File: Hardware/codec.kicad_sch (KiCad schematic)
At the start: 6 parts

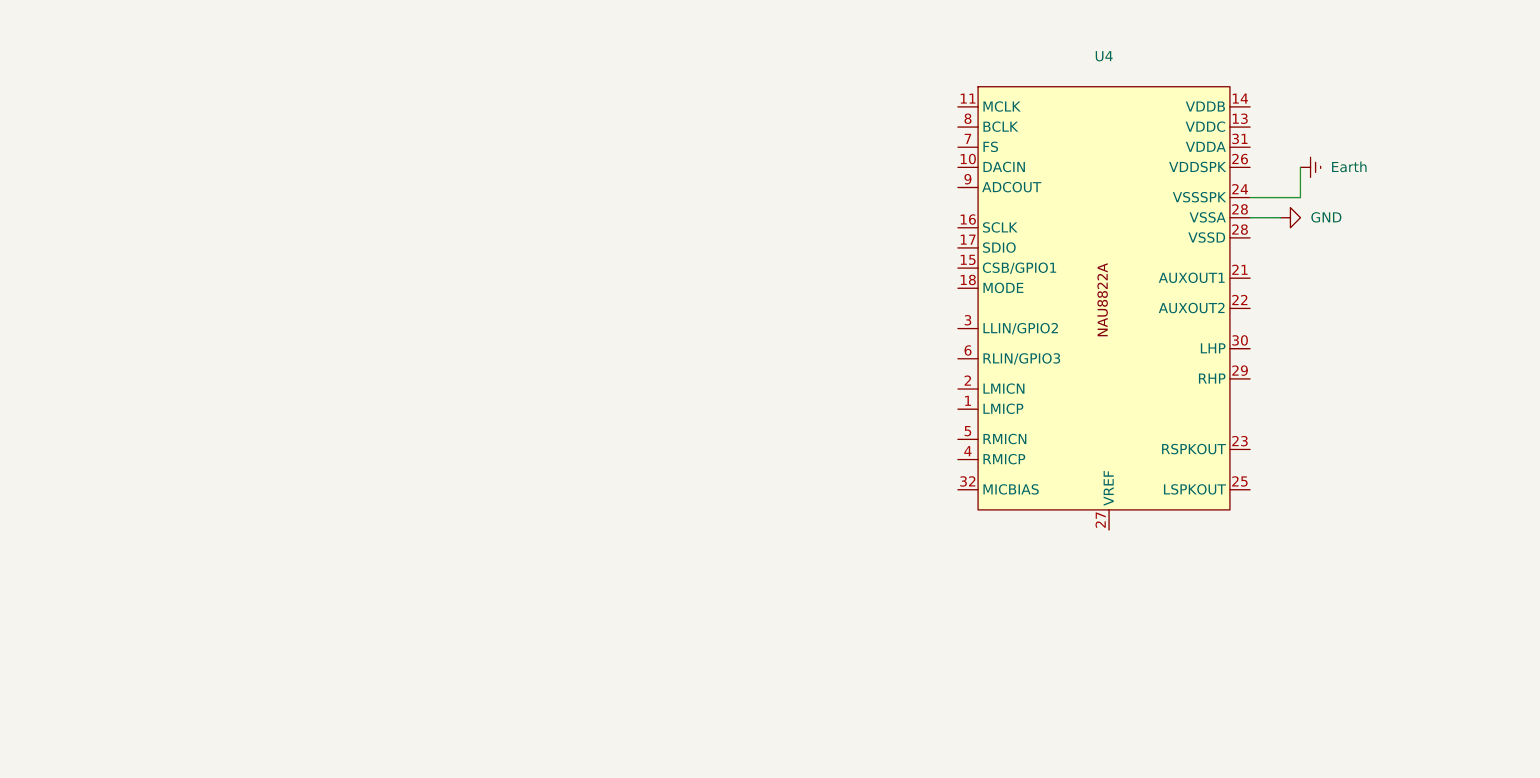
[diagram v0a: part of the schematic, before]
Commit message: CODEC schematics
Missing mic ins and all audio outputs.
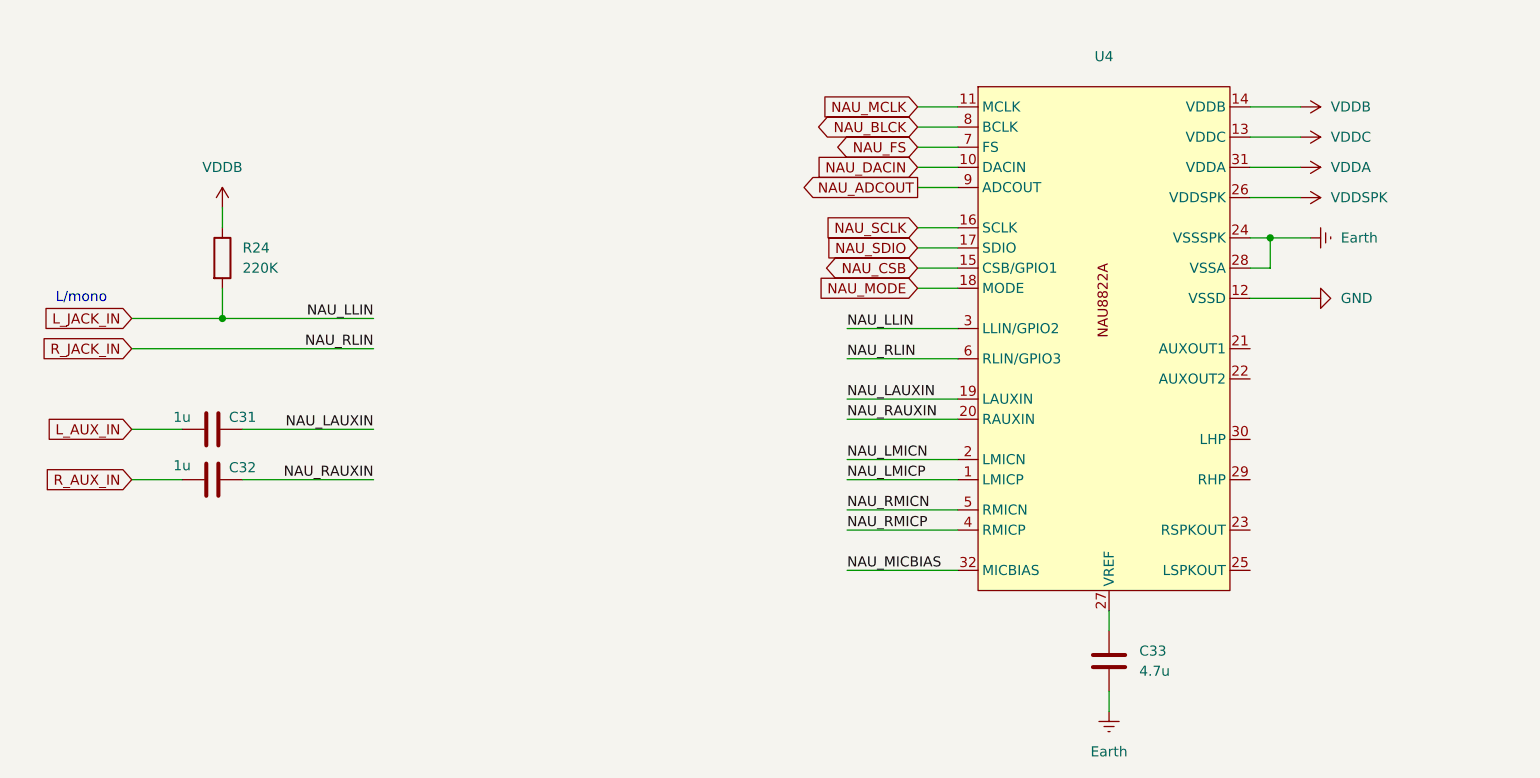
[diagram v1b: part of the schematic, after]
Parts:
- added C31, C32: 1u, symbol Device:C
- added C33: 4.7u, symbol Device:C
- added R24: 220K, symbol Device:R
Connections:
- net Earth: now also U4.28 (VSSA), C33.2
- net GND: now also U4.12 (VSSD); no longer U4.28 (VSSD)
- net VDDA: now also U4.31 (VDDA)
- net VDDB: now also U4.14 (VDDB), R24.1
- net VDDC: now also U4.13 (VDDC)
- net VDDSPK: now also U4.26 (VDDSPK)
- net NAU_LMICP: now reaches U4.1 (LMICP)
- net NAU_DACIN: now reaches U4.10 (DACIN)
- net NAU_MCLK: now reaches U4.11 (MCLK)
- net NAU_CSB: now reaches U4.15 (CSB/GPIO1)
- net NAU_SCLK: now reaches U4.16 (SCLK)
- net NAU_SDIO: now reaches U4.17 (SDIO)
- net NAU_MODE: now reaches U4.18 (MODE)
- net NAU_LMICN: now reaches U4.2 (LMICN)
- net at U4.27 (VREF): now also C33.1
- net L_JACK_IN: now reaches U4.3 (LLIN/GPIO2)
- net L_JACK_IN: now also R24.2
- net NAU_MICBIAS: now reaches U4.32 (MICBIAS)
- net NAU_RMICP: now reaches U4.4 (RMICP)
- net NAU_RMICN: now reaches U4.5 (RMICN)
- net R_JACK_IN: now reaches U4.6 (RLIN/GPIO3)
- net NAU_FS: now reaches U4.7 (FS)
- net NAU_BLCK: now reaches U4.8 (BCLK)
- net NAU_ADCOUT: now reaches U4.9 (ADCOUT)
- new net L_AUX_IN: C31.1
- new net NAU_LAUXIN: C31.2, U4.19 (LAUXIN)
- new net NAU_RAUXIN: C32.2, U4.20 (RAUXIN)
- new net R_AUX_IN: C32.1
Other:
- note added: "L/mono"

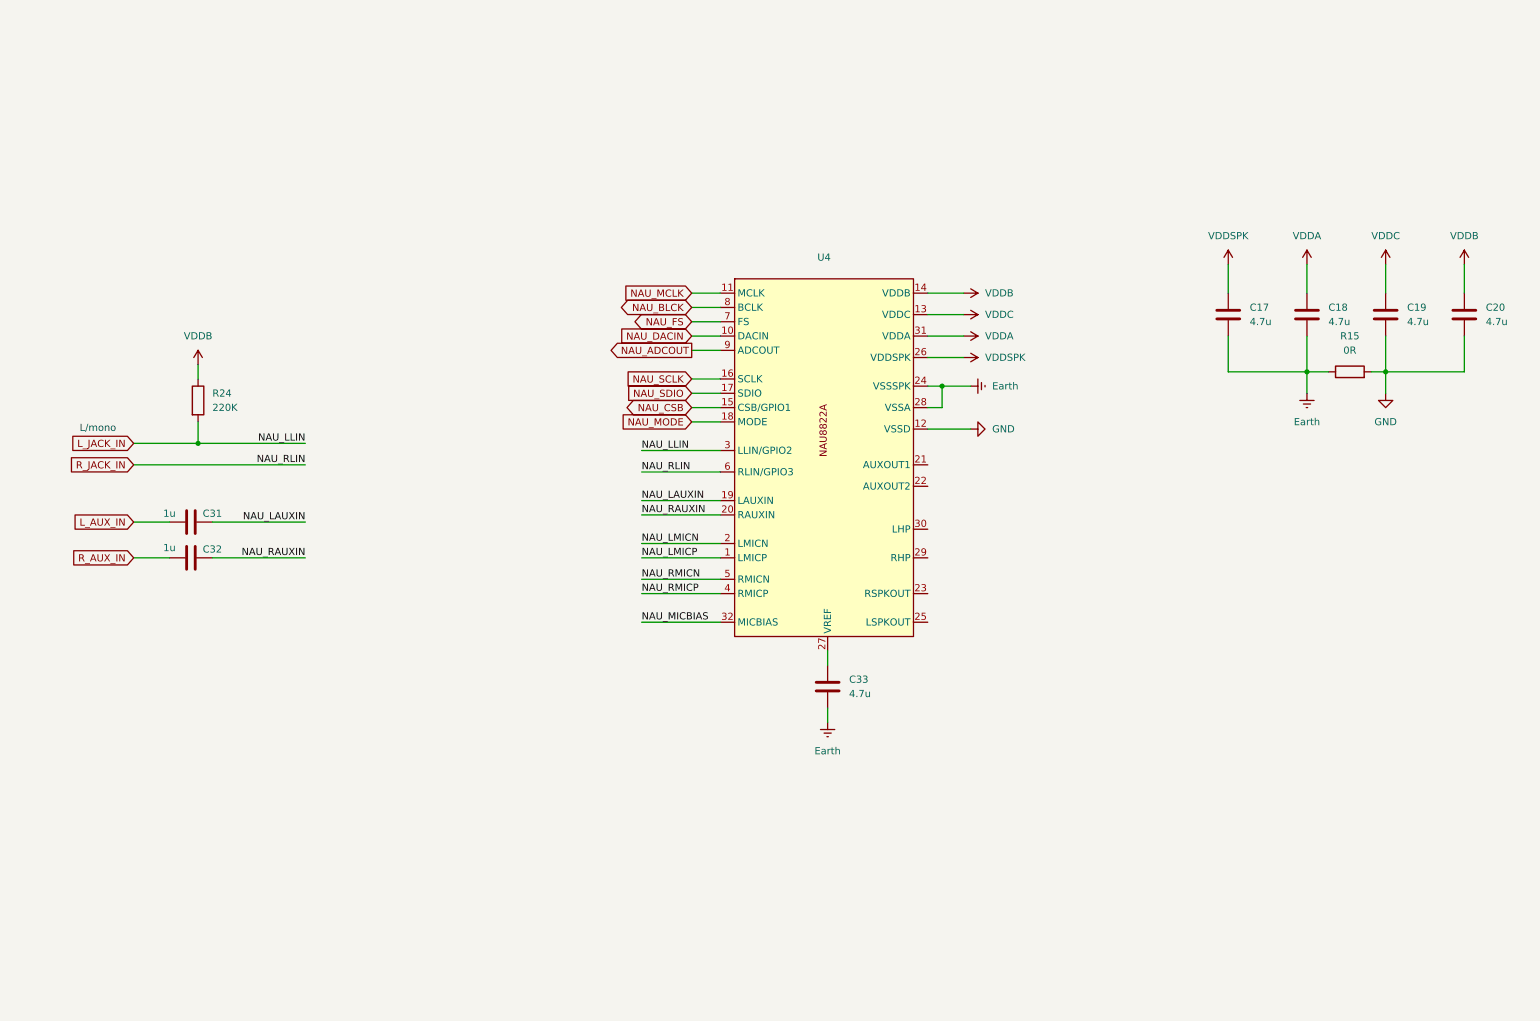
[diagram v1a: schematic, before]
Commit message: Codec schem ready for review
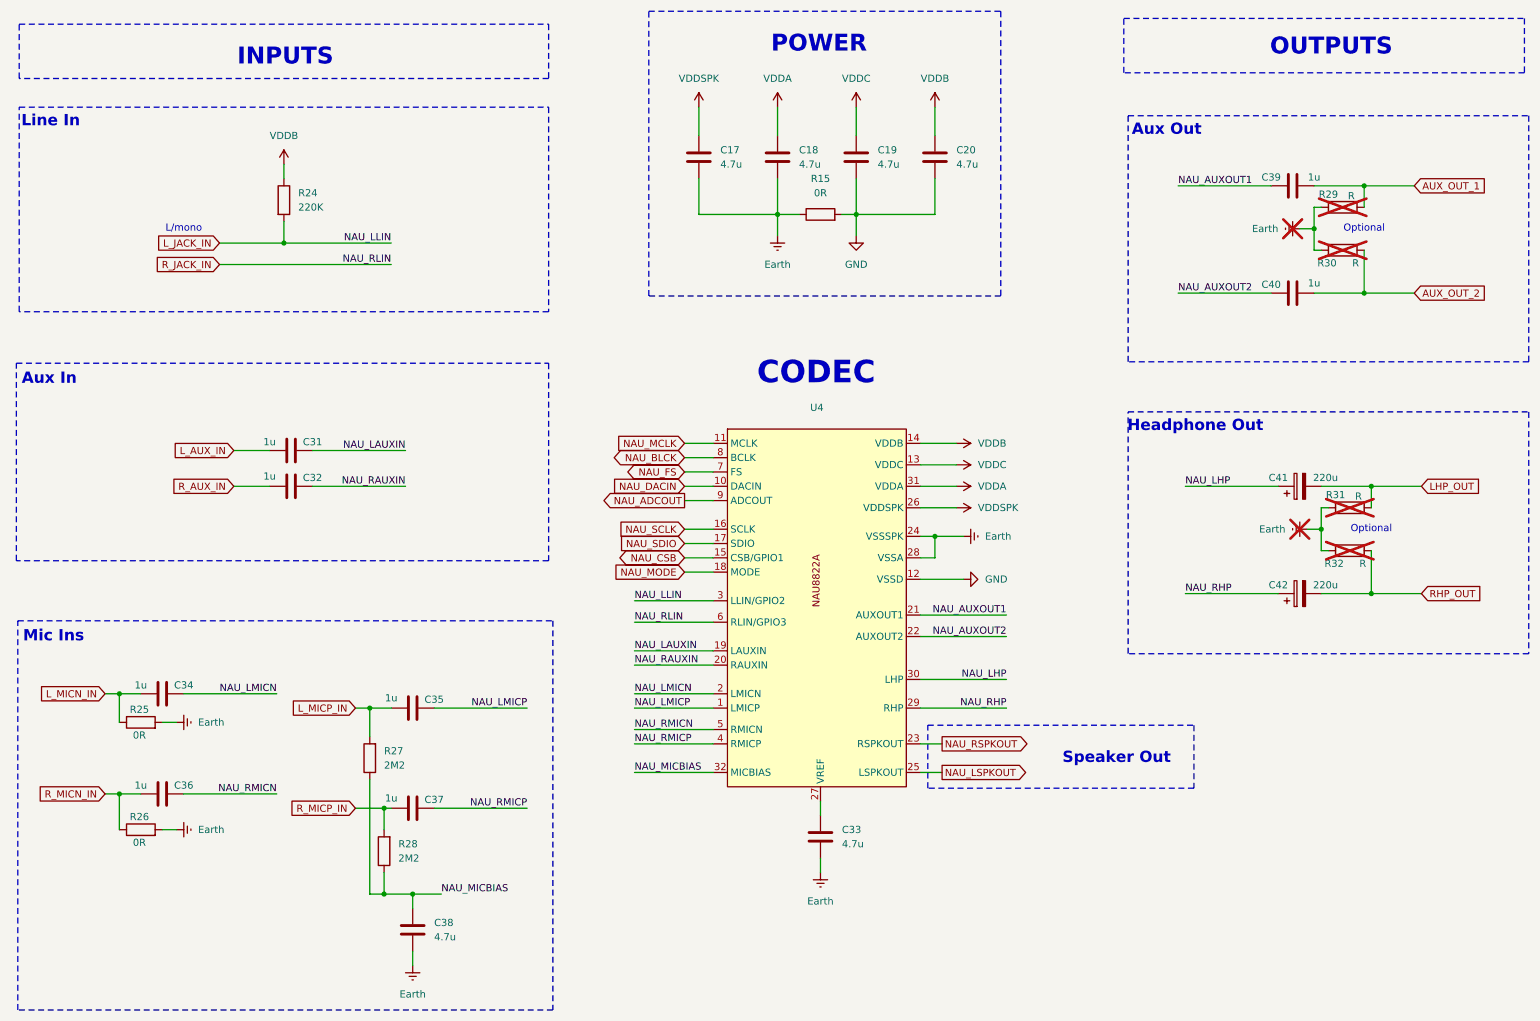
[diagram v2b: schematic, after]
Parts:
- added C34, C35, C36, C37, C39, C40: 1u, symbol Device:C
- added C38: 4.7u, symbol Device:C
- added C41, C42: 220u, symbol Device:C_Polarized
- added R25, R26: 0R, symbol Device:R
- added R27, R28: 2M2, symbol Device:R
- added R29, R30, R31, R32: R, symbol Device:R
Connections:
- net Earth: now also C38.2, R25.2, R26.2, R29.1, R30.1, R31.1, R32.1
- net NAU_LMICN: now also C34.2
- net NAU_LMICP: now also C35.2
- net NAU_MICBIAS: now also C38.1, R27.1, R28.1
- net NAU_RMICN: now also C36.2
- net NAU_RMICP: now also C37.2
- net NAU_AUXOUT1: now reaches U4.21 (AUXOUT1)
- net NAU_AUXOUT1: now also C39.2
- net NAU_AUXOUT2: now reaches U4.22 (AUXOUT2)
- net NAU_AUXOUT2: now also C40.2
- net NAU_RSPKOUT: now reaches U4.23 (RSPKOUT)
- net NAU_LSPKOUT: now reaches U4.25 (LSPKOUT)
- net NAU_RHP: now reaches U4.29 (RHP)
- net NAU_RHP: now also C42.1
- net NAU_LHP: now reaches U4.30 (LHP)
- net NAU_LHP: now also C41.1
- new net AUX_OUT_1: C39.1, R29.2
- new net AUX_OUT_2: C40.1, R30.2
- new net LHP_OUT: C41.2, R31.2
- new net L_MICN_IN: C34.1, R25.1
- new net L_MICP_IN: C35.1, R27.2
- new net RHP_OUT: C42.2, R32.2
- new net R_MICN_IN: C36.1, R26.1
- new net R_MICP_IN: C37.1, R28.2
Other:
- note added: "Aux In"
- note added: "Aux Out"
- note added: "CODEC"
- note added: "Headphone Out"
- note added: "INPUTS"
- note added: "Line In"
- note added: "Mic Ins"
- note added: "OUTPUTS"
- note added: "Optional"
- note added: "POWER"
- note added: "Speaker Out"
- moved on the sheet: C17, C18, C19, C20, C31, C32, C33, R15, R24, U4
